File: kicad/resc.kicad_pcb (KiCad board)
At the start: 4 copper layers, 51 x 75 mm, 167 parts, among them J1 CAN, J10 Conn_Coaxial, J2 HALL, J3 COMM, J4 POWER BTN, J5 SERVO, J6 SWD, J7 LED1, J8 LED2, J9 USB_C_Receptacle_USB2.0_14P, Q1 IRF7749L1, Q2 IRF7749L1, Q3 IRF7749L1, Q4 IRF7749L1, Q5 IRF7749L1, Q6 IRF7749L1, Q7 DMN62D0UW-7, SW1 SENSOR_VOLTAGE, U1 STM32F405RGTx, U10 AD8418, U11 SN74LVC1G66DCKR, U12 SN74LVC1G66DCKR, U13 SN74LVC1G66DCKR, U14 TC2117-3.3VDBTR, U15 USBLC6-2SC6, U16 NRF52832-QFAA-R, U2 TJA1051T-3, U3 SN74LVC1G66DCKR, U5 SN74LVC1G66DCKR, U6 SN74LVC1G66DCKR, U7 BMI160, U8 AD8418, U9 AD8418, Y1 8MHz, Y2 32MHz

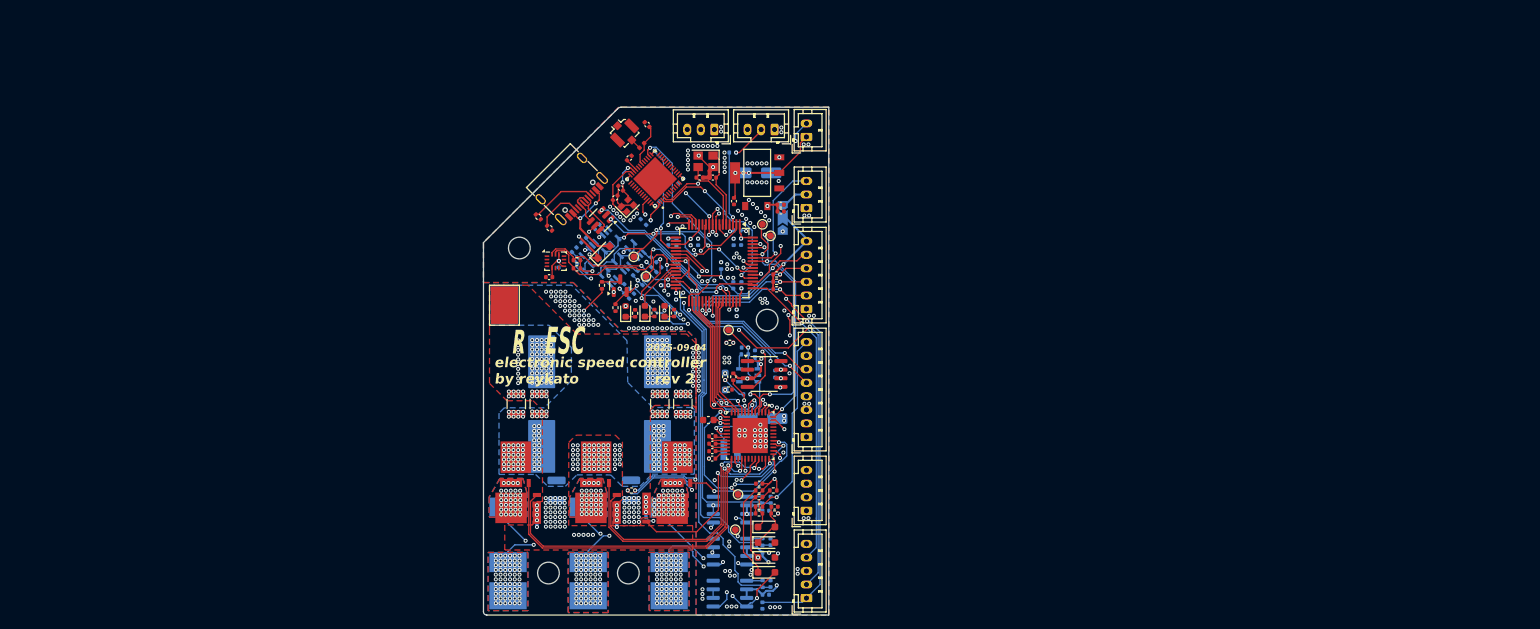
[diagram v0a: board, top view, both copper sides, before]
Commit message: gate driver mostly schematic'd and pcb started
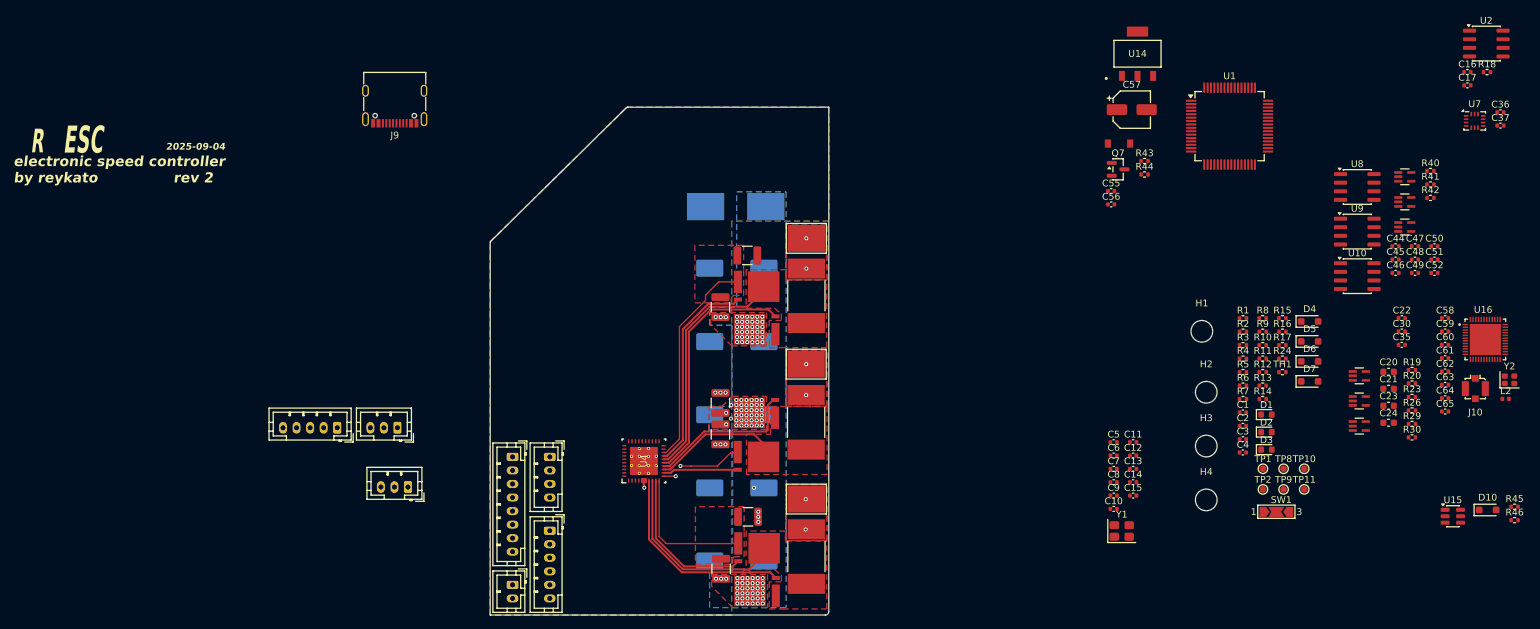
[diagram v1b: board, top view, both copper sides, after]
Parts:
- removed C18: 47uF, Capacitor_SMD:CP_Elec_5x5.3
- removed C19: 1uF, Capacitor_SMD:C_0402_1005Metric
- removed C54: 470uF 63V, footprints:CP_Elec_16x17.5_Panasonic
- removed C66: 2.2uF, Capacitor_SMD:C_0402_1005Metric
- removed D8: 3.6V, Diode_SMD:D_SOD-323_HandSoldering
- removed J8: LED2, Connector_JST:JST_PH_B3B-PH-K_1x03_P2.00mm_Vertical
- removed L1: 22uH, footprints:IND_VLS3010CX-220M-1
- removed R21, R49, R50: 10k, Resistor_SMD:R_0402_1005Metric
- removed R22, R25: 0R, Resistor_SMD:R_0402_1005Metric
- removed R51: 5.1k, Resistor_SMD:R_0402_1005Metric
- removed TP12: nBRAKE, TestPoint:TestPoint_Pad_D1.0mm
- removed U17: ~, footprints:SOT-23-5-DBV_TEX
- added C23: 2.2uF 10V, Capacitor_SMD:C_0603_1608Metric, F.Cu at (253.7, 89.1)
- added C26: 220uF 63V, Capacitor_SMD:CP_Elec_10x10, B.Cu at (157.4, 68.8)
- added C27: 220uF 63V, Capacitor_SMD:CP_Elec_10x10, B.Cu at (157.4, 79.6)
- added C28: 220uF 63V, Capacitor_SMD:CP_Elec_10x10, B.Cu at (157.4, 90.4)
- C1, C10, C11, C14, C15, C17, C2, C22, C30, C35, C37, C38, C40, C44, C45, C46, C47, C48, C49, C5, C50, C51, C52, C57, C58, C6, C60, C61, C64, C7, C8, C9, R1, R14, R17, R18, R19, R20, R23, R26, R29, R30, R34, R35, R36, R40, R41, R42, R9, SW1, TP4, TP5, TP6, U10, U11, U12, U13, U3, U5, U6, U8, U9: moved to F.Cu
- C20: value 1uF -> 100nF; footprint Capacitor_SMD:C_0402_1005Metric -> Capacitor_SMD:C_0603_1608Metric
- C21: value 100nF 63V -> 4.7uF 100V
- C24: value 470nF 16V -> 2.2uF 10V; footprint Capacitor_SMD:C_0402_1005Metric -> Capacitor_SMD:C_0603_1608Metric
- C25: value 470nF 16V -> 220uF 63V; footprint Capacitor_SMD:C_0402_1005Metric -> Capacitor_SMD:CP_Elec_10x10; moved to B.Cu
- C53: value 470uF 63V -> 220uF 63V; footprint footprints:CP_Elec_16x17.5_Panasonic -> Capacitor_SMD:CP_Elec_10x10
- NT1, NT2, NT3: footprint NetTie:NetTie-2_SMD_Pad0.5mm -> footprints:NetTie-2_SMD_Pad0.2mm; moved to F.Cu
- TP7: moved to B.Cu
- U4: value ~ -> DRV8320RSRHAR; footprint footprints:QFN48P700X700X90 -> footprints:RHA0040B
- moved R45 150.4 mm to (272.3, 104.0), turned to 0 degrees
- moved R46 148.9 mm to (272.3, 106.0), turned to 0 degrees
- moved C36 142.6 mm to (270.2, 45.8), turned to 0 degrees
- moved C37 140.6 mm to (270.2, 47.7), turned to 0 degrees
- moved U7 137.3 mm to (266.4, 47.0)
- moved D10 136.0 mm to (268.3, 104.5), turned to 0 degrees
- moved U15 133.2 mm to (263.2, 105.4), turned to 0 degrees
- moved L2 133.0 mm to (271.0, 88.1), turned to 0 degrees
- moved Y2 132.8 mm to (271.5, 85.3), turned to 0 degrees
- moved J10 131.2 mm to (266.5, 86.6), turned to 0 degrees
- moved C50 127.1 mm to (260.4, 65.5), turned to 0 degrees
- moved C51 125.7 mm to (260.4, 67.5), turned to 0 degrees
- moved C65 125.3 mm to (262.0, 90.0), turned to 0 degrees
- moved C62 125.2 mm to (262.0, 84.0), turned to 0 degrees
- moved C63 125.1 mm to (262.0, 86.0), turned to 0 degrees
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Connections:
- C20 pad 1: Net-(U4-VCCLS) -> Net-(D8-K)
- C20 pad 2: GND -> Net-(U4-CB)
- C22 pad 1: /Gate Driver/SENS_A -> /Gate Driver/VOLTAGE_A
- C24 pad 1: Net-(U4-CP2L) -> +5V
- C24 pad 2: Net-(U4-CP2H) -> GND
- C25 pad 1: Net-(U4-CP1L) -> /Gate Driver/SUPPLY
- C25 pad 2: Net-(U4-CP1H) -> GND
- C30 pad 1: /Gate Driver/SENS_B -> /Gate Driver/VOLTAGE_B
- C35 pad 1: /Gate Driver/SENS_C -> /Gate Driver/VOLTAGE_C
- R19 pad 1: /Gate Driver/SENS_A -> /Gate Driver/VOLTAGE_A
- R20 pad 1: /Gate Driver/SENS_A -> /Gate Driver/VOLTAGE_A
- R23 pad 1: /Gate Driver/SENS_B -> /Gate Driver/VOLTAGE_B
- R26 pad 1: /Gate Driver/SENS_B -> /Gate Driver/VOLTAGE_B
- R29 pad 1: /Gate Driver/SENS_C -> /Gate Driver/VOLTAGE_C
- R30 pad 1: /Gate Driver/SENS_C -> /Gate Driver/VOLTAGE_C
- TP8 pad 1: /Gate Driver/DRV_BUCK_OUT -> /DRV_BUCK_OUT
- U1 pad 14: /Gate Driver/SENS_A -> /MCU/VOLTAGE_1
- U1 pad 15: /Gate Driver/SENS_B -> /MCU/VOLTAGE_2
- U1 pad 16: /Gate Driver/SENS_C -> /MCU/VOLTAGE_3
- U4 pad 1: /Gate Driver/CS -> GND
- U4 pad 10: /Gate Driver/INH_C -> /Gate Driver/SL_A
- U4 pad 11: /Gate Driver/INL_C -> /Gate Driver/SL_B
- U4 pad 12: unconnected-(U4-CS_GAIN-Pad12) -> /Gate Driver/GL_B
- U4 pad 13: Net-(D8-K) -> /Gate Driver/SH_B
- U4 pad 14: Net-(U4-DVDD) -> /Gate Driver/GH_B
- U4 pad 15: /Gate Driver/SUPPLY -> /Gate Driver/GH_C
- U4 pad 16: Net-(U4-PH) -> /Gate Driver/SH_C
- U4 pad 17: GND -> /Gate Driver/GL_C
- U4 pad 18: /Gate Driver/DRV_BUCK_OUT -> /Gate Driver/SL_C
- U4 pad 19: Net-(U4-CP1L) -> GND
- U4 pad 2: /Gate Driver/SCK -> Net-(U4-CPL)
- U4 pad 20: Net-(U4-CP1H) -> /Gate Driver/nFAULT
- U4 pad 21: Net-(U4-CP2L) -> /Gate Driver/SDO
- U4 pad 22: Net-(U4-CP2H) -> /Gate Driver/SDI
- U4 pad 23: Net-(U4-VCCLS) -> /Gate Driver/SCK
- U4 pad 24: Net-(U4-VCCHS) -> /Gate Driver/CS
- U4 pad 25: /Gate Driver/GH_C -> /Gate Driver/EN_GATE
- U4 pad 26: /Gate Driver/SH_C -> GND
- U4 pad 27: (no net) -> VDD
- U4 pad 28: /Gate Driver/GL_C -> /Gate Driver/INH_A
- U4 pad 29: /Gate Driver/SL_C -> /Gate Driver/INL_A
- U4 pad 3: /Gate Driver/SDO -> Net-(U4-CPH)
- U4 pad 30: GND -> /Gate Driver/INH_B
- U4 pad 31: GND -> /Gate Driver/INL_B
- U4 pad 32: /Gate Driver/SL_B -> /Gate Driver/INH_C
- U4 pad 33: /Gate Driver/GL_B -> /Gate Driver/INL_C
- U4 pad 34: (no net) -> GND
- U4 pad 35: /Gate Driver/SH_B -> Net-(U4-CB)
- U4 pad 36: /Gate Driver/GH_B -> Net-(D8-K)
- U4 pad 37: /Gate Driver/GH_A -> unconnected-(U4-NC-Pad37)
- U4 pad 38: /SH_A -> /Gate Driver/SUPPLY
- U4 pad 39: (no net) -> /Gate Driver/EN_DRV
- U4 pad 4: /Gate Driver/SDI -> Net-(U4-VCP)
- U4 pad 40: /Gate Driver/GL_A -> Net-(U4-FB)
- U4 pad 41: /Gate Driver/SL_A -> GND
- U4 pad 5: /Gate Driver/nFAULT -> /Gate Driver/SUPPLY
- U4 pad 6: /Gate Driver/INH_A -> /Gate Driver/SUPPLY
- U4 pad 7: /Gate Driver/INL_A -> /Gate Driver/GH_A
- U4 pad 8: /Gate Driver/INH_B -> /SH_A
- U4 pad 9: /Gate Driver/INL_B -> /Gate Driver/GL_A
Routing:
- net VDD: track 268.6 -> 0.00 mm, vias 26 -> 0
- net +5V: track 165.0 -> 0.00 mm, vias 9 -> 0
- net /MCU/CURRENT_1: track 93.2 -> 0.00 mm, vias 4 -> 0
- net /MCU/CURRENT_2: track 81.7 -> 0.00 mm, vias 4 -> 0
- net /MCU/CURRENT_3: track 81.4 -> 0.00 mm, vias 5 -> 0
- net /MCU/NRST: track 71.3 -> 0.00 mm, vias 3 -> 0
- net /Gate Driver/SH_B: track 83.4 -> 19.4 mm, vias 39 -> 0
- net /CONN_SW: track 61.1 -> 0.00 mm, vias 2 -> 0
- net /Gate Driver/SH_C: track 96.3 -> 35.3 mm, vias 38 -> 0
- net /SH_A: track 87.2 -> 28.8 mm, vias 51 -> 0
- net /MCU/SWDIO: track 57.2 -> 0.00 mm, vias 3 -> 0
- net /SHUTDOWN: track 55.6 -> 0.00 mm, vias 3 -> 0
- net /TEMP: track 53.1 -> 0.00 mm, vias 3 -> 0
- net /MCU/SWCLK: track 45.5 -> 0.00 mm, vias 1 -> 0
- net /MOSFETs/PH_C: track 40.1 -> 0.00 mm, vias 68 -> 2
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- added copper zone on F.Cu, net /Gate Driver/SUPPLY
- removed copper zone on B.Cu, net /Gate Driver/SH_B
- removed copper zone on In2.Cu, net /Gate Driver/SH_B
- removed copper zone on B.Cu, net /Gate Driver/SH_C
- removed copper zone on In2.Cu, net /Gate Driver/SH_C
- removed copper zone on B.Cu, net /SH_A
- removed copper zone on In2.Cu, net /SH_A
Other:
- board size 51 x 75 mm -> 50 x 75 mm

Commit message: missed saving pcb
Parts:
- added C18: 100nF, Capacitor_SMD:C_0402_1005Metric, F.Cu at (14.6, 17.2)
- added C29: 4.7uF 100V, Capacitor_SMD:C_1210_3225Metric, F.Cu at (2.33, 1.62)
- added C31: 4.7uF 100V, Capacitor_SMD:C_1210_3225Metric, F.Cu at (2.33, 5.88)
- added C32: 4.7uF 100V, Capacitor_SMD:C_1210_3225Metric, F.Cu at (2.33, 10.1)
- added C33: 2.2uF, Capacitor_SMD:C_0402_1005Metric, F.Cu at (9.49, 7.54)
- added C34: 2.2uF, Capacitor_SMD:C_0402_1005Metric, F.Cu at (9.49, 9.52)
- added C54: 8pF, Capacitor_SMD:C_0402_1005Metric, F.Cu at (14.6, 25.2)
- added J8: USB_C_Receptacle_USB2.0_14P, Connector_USB:USB_C_Receptacle_G-Switch_GT-USB-7010ASV, F.Cu at (5.34, 19.6)
- added R21: 2.2k, Resistor_SMD:R_0402_1005Metric, F.Cu at (14.6, 15.2)
- added R22: 0.0005R, footprints:RESC10052X105N, F.Cu at (11.4, 3.03)
- added R25: 1k, Resistor_SMD:R_0402_1005Metric, F.Cu at (6.61, 7.55)
- added R27: 1k, Resistor_SMD:R_0402_1005Metric, F.Cu at (6.61, 9.54)
- added R28: 39k, Resistor_SMD:R_0402_1005Metric, F.Cu at (14.6, 21.2)
- added R31: 5.1k, Resistor_SMD:R_0402_1005Metric, F.Cu at (0.95, 25.3)
- C10: value 2.2uF -> 15pF
- C11: value 100nF -> 15pF
- C12, C13: value 15pF -> 2.2uF
- C16: value 2.2uF -> 4.7uF 100V; footprint Capacitor_SMD:C_0402_1005Metric -> Capacitor_SMD:C_1206_3216Metric
- C17: value 2.2uF -> 1uF 63V; footprint Capacitor_SMD:C_0402_1005Metric -> Capacitor_SMD:C_0805_2012Metric
- C21: value 4.7uF 100V -> 100nF; footprint Capacitor_SMD:C_0603_1608Metric -> Capacitor_SMD:C_0402_1005Metric
- C22: value 100nF -> 2.2uF 10V; footprint Capacitor_SMD:C_0402_1005Metric -> Capacitor_SMD:C_0603_1608Metric
- C24: value 2.2uF 10V -> 100nF; footprint Capacitor_SMD:C_0603_1608Metric -> Capacitor_SMD:C_0402_1005Metric
- C25, C26: value 220uF 63V -> 2.2uF; footprint Capacitor_SMD:CP_Elec_10x10 -> Capacitor_SMD:C_0402_1005Metric
- C27, C28: value 220uF 63V -> 4.7uF 100V; footprint Capacitor_SMD:CP_Elec_10x10 -> Capacitor_SMD:C_1210_3225Metric
- C3, C35: value 100nF -> 2.2uF
- C30: value 100nF -> 4.7uF 100V; footprint Capacitor_SMD:C_0402_1005Metric -> Capacitor_SMD:C_1210_3225Metric
- C36, C37: value 2.2uF -> 1nF
- C38: value 4.7uF 100V -> 1nF; footprint Capacitor_SMD:C_1210_3225Metric -> Capacitor_SMD:C_0402_1005Metric
- C39, C40, C41: value 4.7uF 100V -> 15nF; footprint Capacitor_SMD:C_1210_3225Metric -> Capacitor_SMD:C_0402_1005Metric
- C42, C43: value 4.7uF 100V -> 220uF 63V; footprint Capacitor_SMD:C_1210_3225Metric -> Capacitor_SMD:CP_Elec_10x10
- C44, C45, C46: value 2.2uF -> 220uF 63V; footprint Capacitor_SMD:C_0402_1005Metric -> Capacitor_SMD:CP_Elec_10x10
- C47, C48: value 1nF -> 2.2uF
- C49: value 1nF -> 47uF; footprint Capacitor_SMD:C_0402_1005Metric -> Capacitor_SMD:CP_Elec_5x5.4
- C50: value 15nF -> 100nF
- C51: value 15nF -> 8pF
- C52: value 15nF -> 4.7uF
- C53: value 220uF 63V -> 4.7uF; footprint Capacitor_SMD:CP_Elec_10x10 -> Capacitor_SMD:C_0402_1005Metric
- C55: value 2.2uF -> 100pF
- C56: value 2.2uF -> 1uF
- C57: value 47uF -> 0.8pF; footprint Capacitor_SMD:CP_Elec_5x5.4 -> Capacitor_SMD:C_0402_1005Metric
- C9: value 2.2uF -> 100nF
- D5: value D_Schottky -> TVS 5V; footprint Diode_SMD:D_SOD-323_HandSoldering -> footprints:SOD-123FL
- D6: value 3.6v -> D_Schottky
- J9: value USB_C_Receptacle_USB2.0_14P -> Conn_Coaxial; footprint Connector_USB:USB_C_Receptacle_G-Switch_GT-USB-7010ASV -> Connector_Coaxial:U.FL_Molex_MCRF_73412-0110_Vertical
- NT1, NT2, NT3: footprint footprints:NetTie-2_SMD_Pad0.2mm -> NetTie:NetTie-2_SMD_Pad0.5mm
- R10: value 39k -> 1k
- R11: value 1k -> 220R
- R12: value 56k -> 220R
- R14: value 220R -> 39k 60V
- R15: value 1k PTC -> 2.2k
- R16: value 1k PTC -> 39k 60V
- R17: value 220R -> 10k
- R18: value 220R -> 56k
- R19, R29: value 39k 60V -> 2.2k
- R20: value 2.2k -> 39k 60V
- R23: value 39k 60V -> 0.0005R; footprint Resistor_SMD:R_0402_1005Metric -> footprints:RESC10052X105N
- R24: value 0R -> 0.0005R; footprint Resistor_SMD:R_0402_1005Metric -> footprints:RESC10052X105N
- R26: value 2.2k -> 1k
- R30: value 2.2k -> 5.1k
- TP1: value DRV_CE -> BUCK_V
- TP10: value nFAULT -> GND; footprint TestPoint:TestPoint_Pad_D1.0mm -> footprints:TestPoint_Pad_5.5x4.0mm
- TP2: value SENS_FILT -> nFAULT
- TP3: value SUPPLY -> EN_GATE; footprint footprints:TestPoint_Pad_5.5x4.0mm -> TestPoint:TestPoint_Pad_D1.0mm
- TP4: value PH_A -> SENS_FILT; footprint footprints:TestPoint_Pad_5.5x4.0mm -> TestPoint:TestPoint_Pad_D1.0mm
- TP5: value PH_B -> DRV_CE; footprint footprints:TestPoint_Pad_5.5x4.0mm -> TestPoint:TestPoint_Pad_D1.0mm
- TP6: value PH_C -> SUPPLY
- TP7: value GND -> PH_A
- TP8: value BUCK_V -> PH_B; footprint TestPoint:TestPoint_Pad_D1.0mm -> footprints:TestPoint_Pad_5.5x4.0mm
- TP9: value SHUTDOWN -> PH_C; footprint TestPoint:TestPoint_Pad_D1.0mm -> footprints:TestPoint_Pad_5.5x4.0mm
- U4: footprint footprints:RHA0040B -> footprints:RHA0040B_NV
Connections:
- C10 pad 1: VDD -> Net-(U1-PH0)
- C11 pad 1: /MCU/NRST -> Net-(U1-PH1)
- C12 pad 1: Net-(U1-PH0) -> Net-(U1-VCAP_1)
- C13 pad 1: Net-(U1-PH1) -> Net-(U1-VCAP_2)
- C14 pad 1: Net-(U1-VCAP_1) -> +5V
- C15 pad 1: Net-(U1-VCAP_2) -> +5V
- C16 pad 1: +5V -> /Gate Driver/SUPPLY
- C17 pad 1: +5V -> /Gate Driver/SUPPLY
- C17 pad 2: GND -> Net-(U4-VCP)
- C20 pad 1: Net-(D8-K) -> Net-(D4-K)
- C21 pad 1: /Gate Driver/SUPPLY -> /Gate Driver/VOLTAGE_B
- C21 pad 2: GND -> Net-(U5-A)
- C22 pad 1: /Gate Driver/VOLTAGE_A -> +5V
- C22 pad 2: Net-(U3-A) -> GND
- C24 pad 1: +5V -> /Gate Driver/VOLTAGE_C
- C24 pad 2: GND -> Net-(U6-A)
- C25 pad 1: /Gate Driver/SUPPLY -> VDD
- C26 pad 1: /Gate Driver/SUPPLY -> VDD
- C3 pad 1: /DRV_CE -> VDD
- C30 pad 1: /Gate Driver/VOLTAGE_B -> /Gate Driver/SUPPLY
- C30 pad 2: Net-(U5-A) -> GND
- C35 pad 1: /Gate Driver/VOLTAGE_C -> VDD
- C35 pad 2: Net-(U6-A) -> GND
- C36 pad 1: VDD -> /MCU/CURRENT_1
- C37 pad 1: VDD -> /MCU/CURRENT_2
- C38 pad 1: /Gate Driver/SUPPLY -> /MCU/CURRENT_3
- C39 pad 1: /Gate Driver/SUPPLY -> Net-(U11-B)
- C4 pad 1: Net-(D5-A) -> VDD
- C40 pad 1: /Gate Driver/SUPPLY -> Net-(U12-B)
- C41 pad 1: /Gate Driver/SUPPLY -> Net-(U13-B)
- C44 pad 1: VDD -> /Gate Driver/SUPPLY
- C45 pad 1: VDD -> /Gate Driver/SUPPLY
- C46 pad 1: VDD -> /Gate Driver/SUPPLY
- C47 pad 1: /MCU/CURRENT_1 -> +5V
- C48 pad 1: /MCU/CURRENT_2 -> VDD
- C49 pad 1: /MCU/CURRENT_3 -> VDD
- C50 pad 1: Net-(U11-B) -> GND
- C50 pad 2: GND -> VDD
- C51 pad 1: Net-(U12-B) -> GND
- C51 pad 2: GND -> Net-(U16-XC1)
- C52 pad 1: Net-(U13-B) -> GND
- C52 pad 2: GND -> VDD
- C53 pad 1: /Gate Driver/SUPPLY -> GND
- C53 pad 2: GND -> Net-(U16-DEC1)
- C55 pad 1: +5V -> GND
- C55 pad 2: GND -> Net-(U16-DEC3)
- C56 pad 1: VDD -> GND
- C56 pad 2: GND -> Net-(U16-DEC4)
- C57 pad 1: VDD -> Net-(U16-ANT)
- C9 pad 1: VDD -> /MCU/NRST
- D4 pad 2: /SH_A -> GND
- D5 pad 1: Net-(D5-K) -> +5V
- D5 pad 2: Net-(D5-A) -> GND
- D6 pad 1: /DRV_CE -> +5V
- D6 pad 2: GND -> Net-(D6-A)
- L2 pad 2: Net-(J10-In) -> Net-(J9-In)
- Q1 pad S: /SH_A -> /Gate Driver/SH_A
- Q4 pad D: /SH_A -> /Gate Driver/SH_A
- R10 pad 1: /DRV_CE -> VDD
- R10 pad 2: Net-(D4-K) -> /IMU/SDA
- R11 pad 1: VDD -> unconnected-(R11-Pad1)
- R11 pad 2: /IMU/SDA -> /SHUTDOWN
- R12 pad 1: /DRV_CE -> /MCU/LED1
- R12 pad 2: Net-(D5-K) -> Net-(J7-Pin_2)
- R13 pad 1: Net-(D5-A) -> /CAN/CANH
- R13 pad 2: /SHUTDOWN -> /CAN/CANL
- R14 pad 1: /MCU/LED1 -> /Gate Driver/VOLTAGE_A
- R14 pad 2: Net-(J7-Pin_2) -> /Gate Driver/SH_A
- R15 pad 1: Net-(D5-K) -> /Gate Driver/VOLTAGE_A
- R15 pad 2: Net-(R15-Pad2) -> GND
- R16 pad 1: /CONN_SW -> /Gate Driver/VOLTAGE_B
- R16 pad 2: Net-(R15-Pad2) -> /Gate Driver/SH_B
- R17 pad 1: /MCU/LED2 -> Net-(U4-FB)
- R17 pad 2: Net-(J8-Pin_2) -> GND
- R18 pad 1: /CAN/CANH -> Net-(U4-FB)
- R18 pad 2: /CAN/CANL -> Net-(D4-K)
- R19 pad 1: /Gate Driver/VOLTAGE_A -> /Gate Driver/VOLTAGE_B
- R19 pad 2: /SH_A -> GND
- R20 pad 1: /Gate Driver/VOLTAGE_A -> /Gate Driver/VOLTAGE_C
- R20 pad 2: GND -> /Gate Driver/SH_C
- R23 pad 1: /Gate Driver/VOLTAGE_B -> /Gate Driver/SH_B
- R23 pad 2: /Gate Driver/SH_B -> /MOSFETs/PH_B
- R24 pad 1: Net-(D5-K) -> /Gate Driver/SH_C
- R24 pad 2: /DRV_CE -> /MOSFETs/PH_C
- R26 pad 1: /Gate Driver/VOLTAGE_B -> /MCU/CURRENT_2
- R26 pad 2: GND -> /MOSFETs/C_B
- R29 pad 1: /Gate Driver/VOLTAGE_C -> /MCU/AN_IN
- R29 pad 2: /Gate Driver/SH_C -> GND
- R30 pad 1: /Gate Driver/VOLTAGE_C -> Net-(J8-CC1)
- TP1 pad 1: /DRV_CE -> /DRV_BUCK_OUT
- TP10 pad 1: /Gate Driver/nFAULT -> GND
- TP2 pad 1: /Gate Driver/SENS_FILTERED -> /Gate Driver/nFAULT
- TP3 pad 1: /Gate Driver/SUPPLY -> /Gate Driver/EN_GATE
- TP4 pad 1: /MOSFETs/PH_A -> /Gate Driver/SENS_FILTERED
- TP5 pad 1: /MOSFETs/PH_B -> /DRV_CE
- TP6 pad 1: /MOSFETs/PH_C -> /Gate Driver/SUPPLY
- TP7 pad 1: GND -> /MOSFETs/PH_A
- TP8 pad 1: /DRV_BUCK_OUT -> /MOSFETs/PH_B
- TP9 pad 1: /SHUTDOWN -> /MOSFETs/PH_C
- U1 pad 4: /MCU/LED2 -> unconnected-(U1-PC15-Pad4)
- U15 pad 4: Net-(J9-D+-PadA6) -> Net-(J8-D+-PadA6)
- U15 pad 6: Net-(J9-D--PadA7) -> Net-(J8-D--PadA7)
- U4 pad 36: Net-(D8-K) -> Net-(D4-K)
- U4 pad 8: /SH_A -> /Gate Driver/SH_A
- U8 pad 8: /SH_A -> /Gate Driver/SH_A
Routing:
- net /SH_A: track 28.8 -> 0.00 mm
- net /Gate Driver/SH_A: track 0.00 -> 28.8 mm
- net /MOSFETs/PH_C: vias 2 -> 1
- net /MOSFETs/PH_B: vias 2 -> 1
- net /Gate Driver/SUPPLY: vias 123 -> 124
- net /DRV_CE: vias 0 -> 1
- added copper zone on F.Cu, net /Gate Driver/SH_A
- added copper zone on In1.Cu, net /Gate Driver/SH_A
- removed copper zone on F.Cu, net /SH_A
- removed copper zone on In1.Cu, net /SH_A

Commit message: rev3 ordered
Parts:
- removed C29, C31, C32: 4.7uF 100V, Capacitor_SMD:C_1210_3225Metric
- removed C33, C34, C4: 2.2uF, Capacitor_SMD:C_0402_1005Metric
- removed C54: 8pF, Capacitor_SMD:C_0402_1005Metric
- removed C57: 0.8pF, Capacitor_SMD:C_0402_1005Metric
- removed D4, D6, D7: D_Schottky, Diode_SMD:D_SOD-323_HandSoldering
- removed D5, D9: TVS 5V, footprints:SOD-123FL
- removed H1, H2, H3, H4: MountingHole, MountingHole:MountingHole_3.2mm_M3
- removed J8: USB_C_Receptacle_USB2.0_14P, Connector_USB:USB_C_Receptacle_G-Switch_GT-USB-7010ASV
- removed R15: 2.2k, Resistor_SMD:R_0402_1005Metric
- removed R16: 39k 60V, Resistor_SMD:R_0402_1005Metric
- removed R17: 10k, Resistor_SMD:R_0402_1005Metric
- removed R24: 0.0005R, footprints:RESC10052X105N
- removed R25, R27: 1k, Resistor_SMD:R_0402_1005Metric
- removed R28: 39k, Resistor_SMD:R_0402_1005Metric
- removed R31: 5.1k, Resistor_SMD:R_0402_1005Metric
- removed TP9: PH_C, footprints:TestPoint_Pad_5.5x4.0mm
- added C19: 1uF 63V, Capacitor_SMD:C_0805_2012Metric, F.Cu at (143.4, 103.8)
- added D8: D_Schottky, Diode_SMD:D_SOD-323_HandSoldering, F.Cu at (138.8, 99.1)
- added L1: 22uH, footprints:IND_VLS3010CX-220M-1, F.Cu at (135.9, 98.9)
- added NT4: NetTie_2, footprints:NetTie-2_SMD_Pad0.2mm, F.Cu at (156.9, 118.3)
- added Q8: DMG3415U, Package_TO_SOT_SMD:SOT-23-3, B.Cu at (138.8, 115.5)
- C1, C14, C15, C2, C5, C58, C6, C60, C61, C63, C64, C7, C8, D1, D2, D3, Q7, R1, R2, R3, R4, R43, R44, R5, R6, R7, R8, R9, SW1, U11, U12, U13, U14, U2: moved to B.Cu
- C10: value 15pF -> 2.2uF; moved to B.Cu
- C11: value 15pF -> 100nF; moved to B.Cu
- C12, C13: value 2.2uF -> 15pF
- C16: value 4.7uF 100V -> 2.2uF; footprint Capacitor_SMD:C_1206_3216Metric -> Capacitor_SMD:C_0402_1005Metric
- C17: value 1uF 63V -> 2.2uF; footprint Capacitor_SMD:C_0805_2012Metric -> Capacitor_SMD:C_0402_1005Metric
- C18: value 100nF -> 47nF
- C20, C23: footprint Capacitor_SMD:C_0603_1608Metric -> Capacitor_SMD:C_0402_1005Metric
- C21: value 100nF -> 4.7uF 100V; footprint Capacitor_SMD:C_0402_1005Metric -> Capacitor_SMD:C_1210_3225Metric
- C22: value 2.2uF 10V -> 100nF; footprint Capacitor_SMD:C_0603_1608Metric -> Capacitor_SMD:C_0402_1005Metric
- C24: value 100nF -> 2.2uF 10V
- C25, C26: value 2.2uF -> 220uF 63V; footprint Capacitor_SMD:C_0402_1005Metric -> Capacitor_SMD:CP_Elec_10x10
- C27, C28: value 4.7uF 100V -> 220uF 63V; footprint Capacitor_SMD:C_1210_3225Metric -> Capacitor_SMD:CP_Elec_10x10
- C3: value 2.2uF -> 100nF; moved to B.Cu
- C30: value 4.7uF 100V -> 100nF; footprint Capacitor_SMD:C_1210_3225Metric -> Capacitor_SMD:C_0402_1005Metric
- C35: value 2.2uF -> 100nF
- C36, C37: value 1nF -> 2.2uF
- C38: value 1nF -> 4.7uF 100V; footprint Capacitor_SMD:C_0402_1005Metric -> Capacitor_SMD:C_1210_3225Metric
- C39, C40, C41: value 15nF -> 4.7uF 100V; footprint Capacitor_SMD:C_0402_1005Metric -> Capacitor_SMD:C_1210_3225Metric
- C42, C43: value 220uF 63V -> 4.7uF 100V; footprint Capacitor_SMD:CP_Elec_10x10 -> Capacitor_SMD:C_1210_3225Metric
- C44, C45, C46: value 220uF 63V -> 2.2uF; footprint Capacitor_SMD:CP_Elec_10x10 -> Capacitor_SMD:C_0402_1005Metric; moved to B.Cu
- C47, C48: value 2.2uF -> 1nF
- C49: value 47uF -> 1nF; footprint Capacitor_SMD:CP_Elec_5x5.4 -> Capacitor_SMD:C_0402_1005Metric
- C50: value 100nF -> 15nF; moved to B.Cu
- C51: value 8pF -> 15nF; moved to B.Cu
- C52: value 4.7uF -> 15nF; moved to B.Cu
- C53: value 4.7uF -> 220uF 63V; footprint Capacitor_SMD:C_0402_1005Metric -> Capacitor_SMD:CP_Elec_10x10
- C55: value 100pF -> 2.2uF; moved to B.Cu
- C56: value 1uF -> 2.2uF; moved to B.Cu
- C9: value 100nF -> 2.2uF; moved to B.Cu
- J9: value Conn_Coaxial -> USB_C_Receptacle_USB2.0_14P; footprint Connector_Coaxial:U.FL_Molex_MCRF_73412-0110_Vertical -> Connector_USB:USB_C_Receptacle_G-Switch_GT-USB-7010ASV
- NT1, NT2, NT3: footprint NetTie:NetTie-2_SMD_Pad0.5mm -> footprints:NetTie-2_SMD_Pad0.2mm
- R10: value 1k -> 100k
- R11: value 220R -> 1k; moved to B.Cu
- R12: value 220R -> 10k; moved to B.Cu
- R14: value 39k 60V -> 220R; moved to B.Cu
- R18: value 56k -> 220R
- R19, R29: value 2.2k -> 39k 60V
- R20: value 39k 60V -> 2.2k
- R21: value 2.2k -> 56k
- R22: value 0.0005R -> 10k; footprint footprints:RESC10052X105N -> Resistor_SMD:R_0402_1005Metric
- R23: value 0.0005R -> 39k 60V; footprint footprints:RESC10052X105N -> Resistor_SMD:R_0402_1005Metric
- R26: value 1k -> 2.2k
- R30: value 5.1k -> 2.2k
- TP1: value BUCK_V -> nSHDN; moved to B.Cu
- TP10: value GND -> nFAULT; footprint footprints:TestPoint_Pad_5.5x4.0mm -> TestPoint:TestPoint_Pad_D1.0mm; moved to B.Cu
- TP11: value EN_GATE -> EN_DRV
- TP2: value nFAULT -> SENS_FILT
- TP3: value EN_GATE -> SUPPLY; footprint TestPoint:TestPoint_Pad_D1.0mm -> footprints:TestPoint_Pad_5.5x4.0mm
- TP4: value SENS_FILT -> PH_A; footprint TestPoint:TestPoint_Pad_D1.0mm -> footprints:TestPoint_Pad_5.5x4.0mm
- TP5: value DRV_CE -> PH_B; footprint TestPoint:TestPoint_Pad_D1.0mm -> footprints:TestPoint_Pad_5.5x4.0mm
- TP6: value SUPPLY -> PH_C
- TP7: value PH_A -> GND
- TP8: value PH_B -> CONN_SW; footprint footprints:TestPoint_Pad_5.5x4.0mm -> TestPoint:TestPoint_Pad_D1.0mm
- moved R22 162.8 mm to (139.4, 103.6), turned to 90 degrees
- moved R21 153.8 mm to (140.6, 103.6), turned to -90 degrees
- moved C18 153.6 mm to (141.6, 103.6), turned to 90 degrees
- moved R45 149.3 mm to (127.1, 69.0), turned to 135 degrees
- moved R46 147.5 mm to (129.1, 71.0), turned to -45 degrees
- moved C36 145.8 mm to (128.1, 78.5), turned to 180 degrees
- moved U2 145.7 mm to (129.8, 81.2), turned to -90 degrees
- moved R18 145.0 mm to (129.8, 83.1)
- moved C37 142.7 mm to (130.0, 74.0)
- moved C16 142.6 mm to (129.8, 84.1), turned to 180 degrees
- moved C17 141.0 mm to (129.8, 80.7), turned to 180 degrees
- moved U7 140.4 mm to (129.1, 76.3), turned to 180 degrees
- moved D10 137.2 mm to (135.2, 71.2), turned to -135 degrees
- moved R42 136.6 mm to (133.7, 110.8), turned to -90 degrees
- moved Y2 136.6 mm to (137.4, 59.7), turned to 45 degrees
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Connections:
- C10 pad 1: Net-(U1-PH0) -> VDD
- C11 pad 1: Net-(U1-PH1) -> /MCU/NRST
- C12 pad 1: Net-(U1-VCAP_1) -> Net-(U1-PH0)
- C13 pad 1: Net-(U1-VCAP_2) -> Net-(U1-PH1)
- C14 pad 1: +5V -> Net-(U1-VCAP_1)
- C15 pad 1: +5V -> Net-(U1-VCAP_2)
- C16 pad 1: /Gate Driver/SUPPLY -> +5V
- C17 pad 1: /Gate Driver/SUPPLY -> +5V
- C17 pad 2: Net-(U4-VCP) -> GND
- C18 pad 1: /Gate Driver/VOLTAGE_A -> Net-(U4-CPH)
- C18 pad 2: Net-(U3-A) -> Net-(U4-CPL)
- C20 pad 1: Net-(D4-K) -> Net-(D8-K)
- C21 pad 1: /Gate Driver/VOLTAGE_B -> /Gate Driver/SUPPLY
- C21 pad 2: Net-(U5-A) -> GND
- C22 pad 1: +5V -> /Gate Driver/VOLTAGE_A
- C22 pad 2: GND -> Net-(U3-A)
- C24 pad 1: /Gate Driver/VOLTAGE_C -> +5V
- C24 pad 2: Net-(U6-A) -> GND
- C25 pad 1: VDD -> /Gate Driver/SUPPLY
- C26 pad 1: VDD -> /Gate Driver/SUPPLY
- C3 pad 1: VDD -> /CONN_SW
- C30 pad 1: /Gate Driver/SUPPLY -> /Gate Driver/VOLTAGE_B
- C30 pad 2: GND -> Net-(U5-A)
- C35 pad 1: VDD -> /Gate Driver/VOLTAGE_C
- C35 pad 2: GND -> Net-(U6-A)
- C36 pad 1: /MCU/CURRENT_1 -> VDD
- C37 pad 1: /MCU/CURRENT_2 -> VDD
- C38 pad 1: /MCU/CURRENT_3 -> /Gate Driver/SUPPLY
- C39 pad 1: Net-(U11-B) -> /Gate Driver/SUPPLY
- C40 pad 1: Net-(U12-B) -> /Gate Driver/SUPPLY
- C41 pad 1: Net-(U13-B) -> /Gate Driver/SUPPLY
- C44 pad 1: /Gate Driver/SUPPLY -> VDD
- C45 pad 1: /Gate Driver/SUPPLY -> VDD
- C46 pad 1: /Gate Driver/SUPPLY -> VDD
- C47 pad 1: +5V -> /MCU/CURRENT_1
- C48 pad 1: VDD -> /MCU/CURRENT_2
- C49 pad 1: VDD -> /MCU/CURRENT_3
- C50 pad 1: GND -> Net-(U11-B)
- C50 pad 2: VDD -> GND
- C51 pad 1: GND -> Net-(U12-B)
- C51 pad 2: Net-(U16-XC1) -> GND
- C52 pad 1: GND -> Net-(U13-B)
- C52 pad 2: VDD -> GND
- C53 pad 1: GND -> /Gate Driver/SUPPLY
- C53 pad 2: Net-(U16-DEC1) -> GND
- C55 pad 1: GND -> +5V
- C55 pad 2: Net-(U16-DEC3) -> GND
- C56 pad 1: GND -> VDD
- C56 pad 2: Net-(U16-DEC4) -> GND
- C9 pad 1: /MCU/NRST -> VDD
- J4 pad 1: VDD -> GND
- L2 pad 2: Net-(J9-In) -> Net-(J10-In)
- R10 pad 1: VDD -> GND
- R10 pad 2: /IMU/SDA -> /nSHDN
- R11 pad 1: unconnected-(R11-Pad1) -> VDD
- R11 pad 2: /SHUTDOWN -> /IMU/SDA
- R12 pad 1: /MCU/LED1 -> VDD
- R12 pad 2: Net-(J7-Pin_2) -> /CONN_SW
- R13 pad 1: /CAN/CANH -> /nSHDN
- R13 pad 2: /CAN/CANL -> /POWER
- R14 pad 1: /Gate Driver/VOLTAGE_A -> /MCU/LED1
- R14 pad 2: /Gate Driver/SH_A -> Net-(J7-Pin_2)
- R18 pad 1: Net-(U4-FB) -> /CAN/CANH
- R18 pad 2: Net-(D4-K) -> /CAN/CANL
- R19 pad 1: /Gate Driver/VOLTAGE_B -> /Gate Driver/VOLTAGE_A
- R19 pad 2: GND -> /Gate Driver/SH_A
- R20 pad 1: /Gate Driver/VOLTAGE_C -> /Gate Driver/VOLTAGE_A
- R20 pad 2: /Gate Driver/SH_C -> GND
- R21 pad 1: /Gate Driver/VOLTAGE_C -> Net-(U4-FB)
- R21 pad 2: GND -> +5V
- R22 pad 1: /Gate Driver/SH_A -> GND
- R22 pad 2: /MOSFETs/PH_A -> Net-(U4-FB)
- R23 pad 1: /Gate Driver/SH_B -> /Gate Driver/VOLTAGE_B
- R23 pad 2: /MOSFETs/PH_B -> /Gate Driver/SH_B
- R26 pad 1: /MCU/CURRENT_2 -> /Gate Driver/VOLTAGE_B
- R26 pad 2: /MOSFETs/C_B -> GND
- R29 pad 1: /MCU/AN_IN -> /Gate Driver/VOLTAGE_C
- R29 pad 2: GND -> /Gate Driver/SH_C
- R30 pad 1: Net-(J8-CC1) -> /Gate Driver/VOLTAGE_C
- R34 pad 1: /SH_A -> /Gate Driver/SH_A
- TP1 pad 1: /DRV_BUCK_OUT -> /nSHDN
- TP10 pad 1: GND -> /Gate Driver/nFAULT
- TP11 pad 1: /Gate Driver/EN_GATE -> /Gate Driver/EN_DRV
- TP2 pad 1: /Gate Driver/nFAULT -> /Gate Driver/SENS_FILTERED
- TP3 pad 1: /Gate Driver/EN_GATE -> /Gate Driver/SUPPLY
- TP4 pad 1: /Gate Driver/SENS_FILTERED -> /MOSFETs/PH_A
- TP5 pad 1: /DRV_CE -> /MOSFETs/PH_B
- TP6 pad 1: /Gate Driver/SUPPLY -> /MOSFETs/PH_C
- TP7 pad 1: /MOSFETs/PH_A -> GND
- TP8 pad 1: /MOSFETs/PH_B -> /CONN_SW
- U1 pad 14: /MCU/VOLTAGE_1 -> /Gate Driver/VOLTAGE_A
- U1 pad 15: /MCU/VOLTAGE_2 -> /Gate Driver/VOLTAGE_B
- U1 pad 16: /MCU/VOLTAGE_3 -> /Gate Driver/VOLTAGE_C
- U1 pad 25: /SHUTDOWN -> /POWER
- U1 pad 37: /MCU/HALL_1 -> /Gate Driver/INH_A
- U1 pad 38: /MCU/HALL_2 -> /Gate Driver/INH_B
- U1 pad 39: /MCU/HALL_3 -> /Gate Driver/INH_C
- U1 pad 4: unconnected-(U1-PC15-Pad4) -> /CONN_SW
- U1 pad 41: /Gate Driver/INH_A -> /MCU/HALL_1
- U1 pad 42: /Gate Driver/INH_B -> /MCU/HALL_2
- U1 pad 43: /Gate Driver/INH_C -> /MCU/HALL_3
- U1 pad 57: /Gate Driver/EN_GATE -> /Gate Driver/EN_DRV
- U15 pad 4: Net-(J8-D+-PadA6) -> Net-(J9-D+-PadA6)
- U15 pad 6: Net-(J8-D--PadA7) -> Net-(J9-D--PadA7)
- U4 pad 25: /Gate Driver/EN_GATE -> /Gate Driver/EN_DRV
- U4 pad 36: Net-(D4-K) -> Net-(D8-K)
- U4 pad 39: /Gate Driver/EN_DRV -> /nSHDN
- U4 pad 6: /Gate Driver/SUPPLY -> Net-(U4-VDRAIN)
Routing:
- net VDD: track 0.00 -> 232.7 mm, vias 0 -> 27
- net +5V: track 0.00 -> 110.4 mm, vias 0 -> 9
- net /CONN_SW: track 0.00 -> 78.4 mm, vias 0 -> 4
- net /Gate Driver/SH_C: track 35.3 -> 109.3 mm, vias 0 -> 2
- net /MOSFETs/PH_C: track 0.00 -> 66.0 mm, vias 1 -> 2
- net /MCU/CURRENT_1: track 0.00 -> 59.3 mm, vias 0 -> 4
- net /Gate Driver/SENS_FILTERED: track 0.00 -> 59.2 mm, vias 0 -> 2
- net /MCU/CURRENT_2: track 0.00 -> 56.2 mm, vias 0 -> 4
- net /MCU/CURRENT_3: track 0.00 -> 55.2 mm, vias 0 -> 3
- net /Gate Driver/VOLTAGE_A: track 0.00 -> 52.5 mm, vias 0 -> 2
- net /Gate Driver/VOLTAGE_B: track 0.00 -> 51.3 mm, vias 0 -> 2
- net /Gate Driver/SH_B: track 19.4 -> 68.0 mm, vias 0 -> 2
- net /TEMP: track 0.00 -> 44.9 mm, vias 0 -> 3
- net /Gate Driver/VOLTAGE_C: track 0.00 -> 44.3 mm, vias 0 -> 2
- net /MCU/CURR_FILT_ON: track 0.00 -> 43.3 mm, vias 0 -> 3
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- removed copper zone on In1.Cu, net /Gate Driver/SH_A
- removed copper zone on In1.Cu, net /Gate Driver/SH_B
- removed copper zone on In1.Cu, net /Gate Driver/SH_C
- removed copper zone on In2.Cu, net /Gate Driver/SUPPLY
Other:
- board size 50 x 75 mm -> 50 x 66 mm
- board text added: "2025-10-15"
- board text added: "by reykato"
- board text added: "rev 3"
- board text removed: "2025-09-04"
- board text removed: "electronic speed controller by reykato"
- board text removed: "rev 2"
